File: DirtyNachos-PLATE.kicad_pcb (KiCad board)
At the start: 2 copper layers, 20 x 128.5 mm, 10 parts

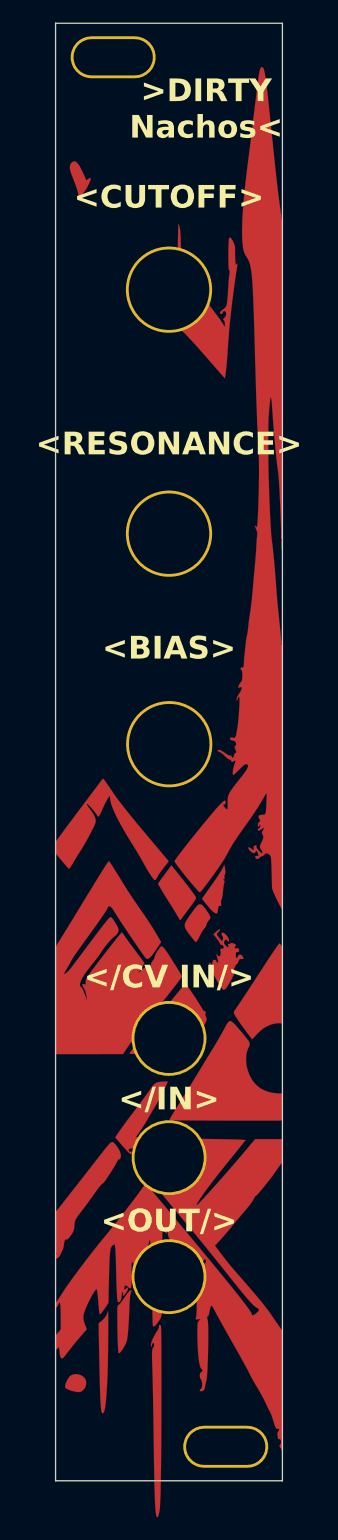
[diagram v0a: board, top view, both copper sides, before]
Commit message: Updates v0.2
Better Faceplate.
New holes now with copper.
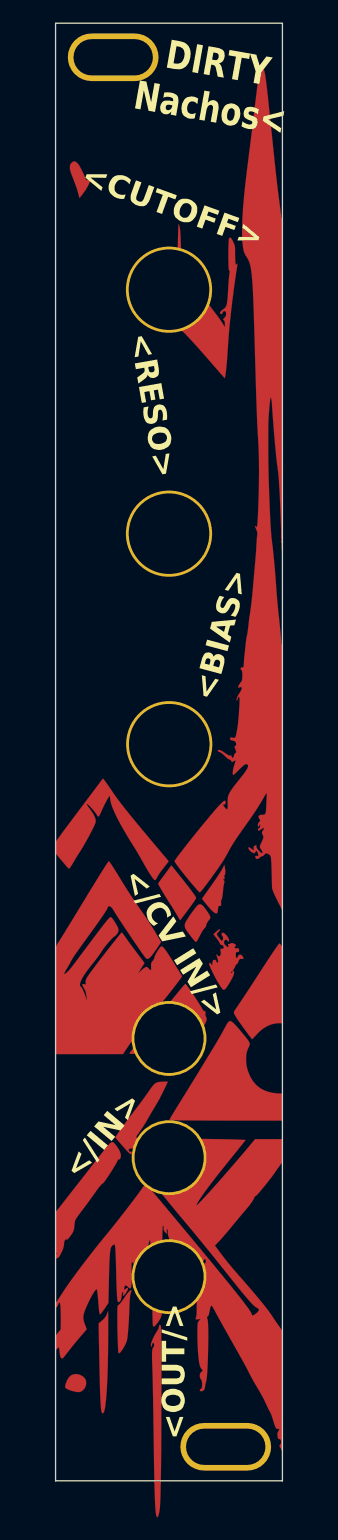
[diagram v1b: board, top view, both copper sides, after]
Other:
- board text added: "<RESO>"
- board text added: "DIRTY Nachos<"
- board text removed: "<RESONANCE>"
- board text removed: ">DIRTY Nachos<"
